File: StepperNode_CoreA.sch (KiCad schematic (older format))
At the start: 1 part

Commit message: Finished DAC interface sheets.
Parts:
- A?: symbol NODE_CORE_CONNECTOR -> NODE_CORE_CONNECTOR-RESCUE-rloopStepperNode
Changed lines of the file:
@@
 EESchema Schematic File Version 2
+LIBS:rloopStepperNode-rescue
 LIBS:power
 LIBS:device
@@
 Original Author: SafetyLok
 $Comp
-L NODE_CORE_CONNECTOR A?
+L NODE_CORE_CONNECTOR-RESCUE-rloopStepperNode A?
 U 1 1 57538837
 P 8150 4600

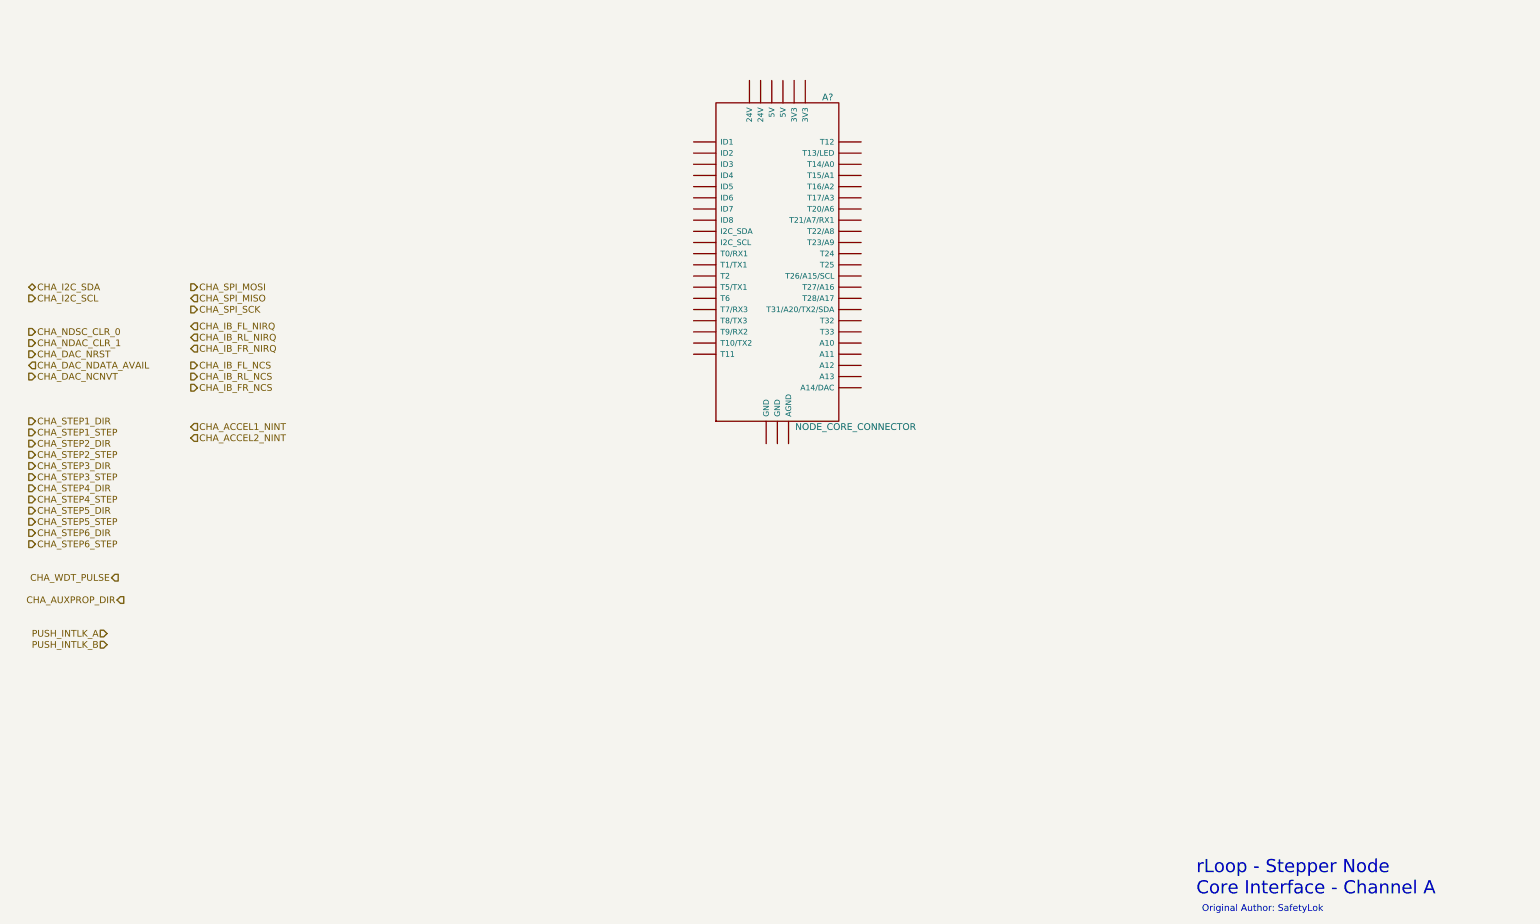
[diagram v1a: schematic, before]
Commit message: Updated node core connector pages and added interlocks.
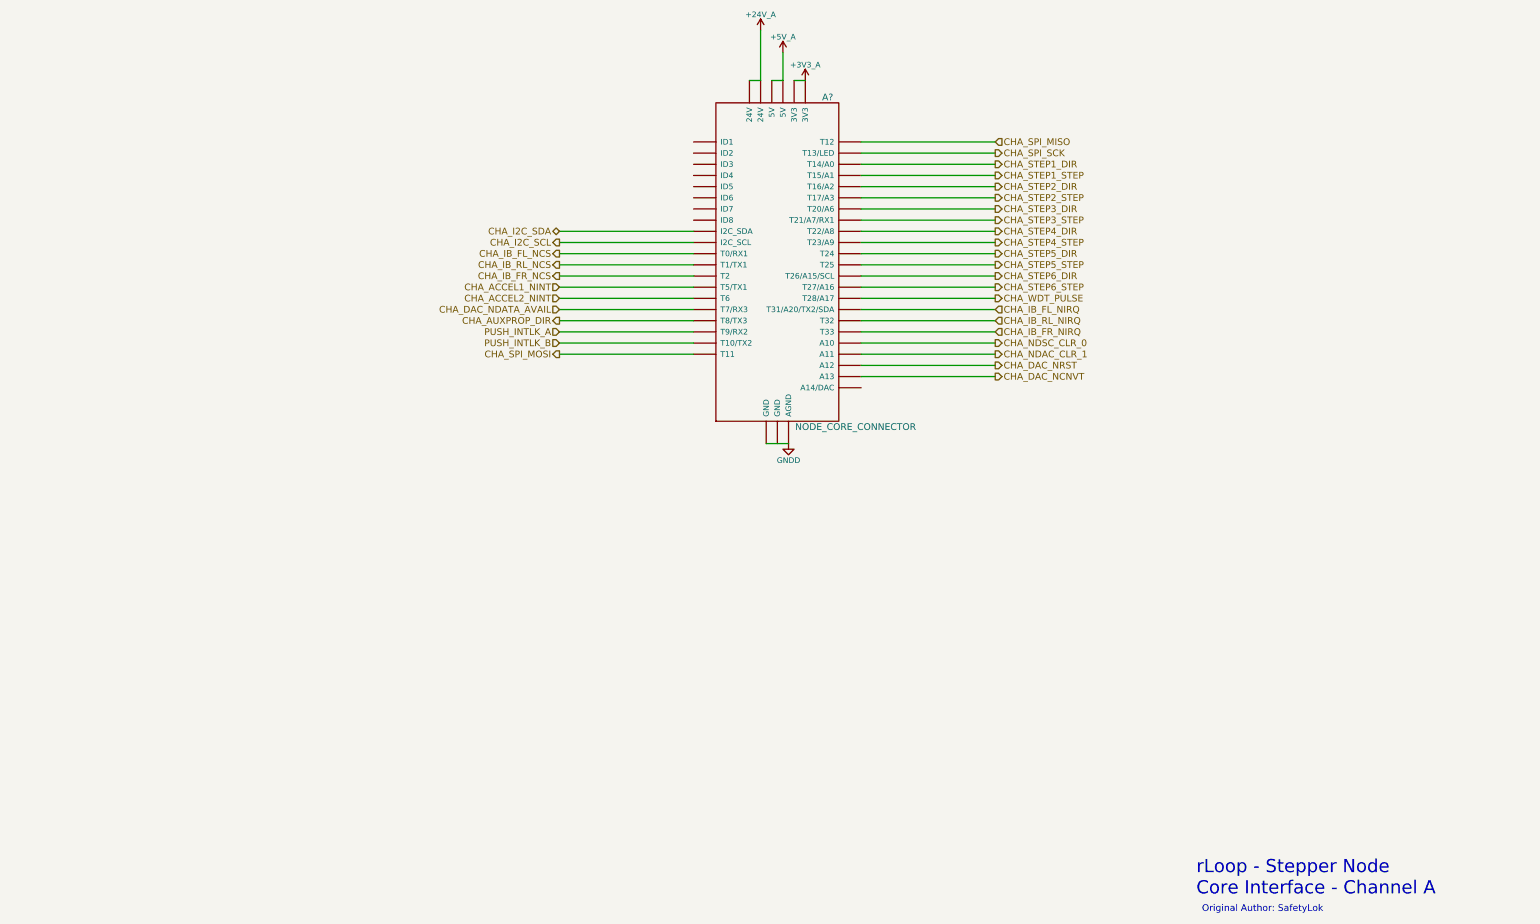
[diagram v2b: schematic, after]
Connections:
- net CHA_ACCEL1_NINT: now also A?.T5 (T5/TX1)
- net CHA_ACCEL2_NINT: now also A?.T6
- net CHA_AUXPROP_DIR: now also A?.T8 (T8/TX3)
- net CHA_DAC_NCNVT: now also A?.A13
- net CHA_DAC_NDATA_AVAIL: now also A?.T7 (T7/RX3)
- net CHA_DAC_NRST: now also A?.A12
- net CHA_I2C_SCL: now also A?.~ (ID8)
- net CHA_I2C_SDA: now also A?.~ (ID8)
- net CHA_IB_FL_NCS: now also A?.T0 (T0/RX1)
- net CHA_IB_FL_NIRQ: now also A?.T31 (T31/A20/TX2/SDA)
- net CHA_IB_FR_NCS: now also A?.T2
- net CHA_IB_FR_NIRQ: now also A?.T33
- net CHA_IB_RL_NCS: now also A?.T1 (T1/TX1)
- net CHA_IB_RL_NIRQ: now also A?.T32
- net CHA_NDAC_CLR_1: now also A?.A11
- net CHA_NDSC_CLR_0: now also A?.A10
- net CHA_SPI_MISO: now also A?.T12
- net CHA_SPI_MOSI: now also A?.T11
- net CHA_SPI_SCK: now also A?.T13 (T13/LED)
- net CHA_STEP1_DIR: now also A?.T14 (T14/A0)
- net CHA_STEP1_STEP: now also A?.T15 (T15/A1)
- net CHA_STEP2_DIR: now also A?.T16 (T16/A2)
- net CHA_STEP2_STEP: now also A?.T17 (T17/A3)
- net CHA_STEP3_DIR: now also A?.T20 (T20/A6)
- net CHA_STEP3_STEP: now also A?.T21 (T21/A7/RX1)
- net CHA_STEP4_DIR: now also A?.T22 (T22/A8)
- net CHA_STEP4_STEP: now also A?.T23 (T23/A9)
- net CHA_STEP5_DIR: now also A?.T24
- net CHA_STEP5_STEP: now also A?.T25
- net CHA_STEP6_DIR: now also A?.T26 (T26/A15/SCL)
- net CHA_STEP6_STEP: now also A?.T27 (T27/A16)
- net CHA_WDT_PULSE: now also A?.T28 (T28/A17)
- net PUSH_INTLK_A: now also A?.T9 (T9/RX2)
- net PUSH_INTLK_B: now also A?.T10 (T10/TX2)
- net +5V: now reaches A?.+24V (24V)
- net +5V: now also A?.+5V (5V)
- net +3V3: now reaches A?.+3V3 (3V3)
- net GNDD: now reaches A?.AGND
- net GNDD: now also A?.GND
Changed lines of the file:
@@
 	1    0    0    -1
 $EndComp
-Text HLabel 1450 4900 2    60   BiDi ~ 0
+Text HLabel 10100 5400 2    60   Output ~ 0
+CHA_NDSC_CLR_0
+Text HLabel 10100 5500 2    60   Output ~ 0
+CHA_NDAC_CLR_1
+Text HLabel 10100 5600 2    60   Output ~ 0
+CHA_DAC_NRST
+Text HLabel 6200 5100 0    60   Input ~ 0
+CHA_DAC_NDATA_AVAIL
+Text HLabel 10100 5700 2    60   Output ~ 0
+CHA_DAC_NCNVT
+Text HLabel 10100 3800 2    60   Output ~ 0
+CHA_STEP1_DIR
+Text HLabel 10100 3900 2    60   Output ~ 0
+CHA_STEP1_STEP
+Text HLabel 10100 4000 2    60   Output ~ 0
+CHA_STEP2_DIR
+Text HLabel 10100 4100 2    60   Output ~ 0
+CHA_STEP2_STEP
+Text HLabel 10100 4200 2    60   Output ~ 0
+CHA_STEP3_DIR
+Text HLabel 10100 4300 2    60   Output ~ 0
+CHA_STEP3_STEP
+Text HLabel 10100 4400 2    60   Output ~ 0
+CHA_STEP4_DIR
+Text HLabel 10100 4500 2    60   Output ~ 0
+CHA_STEP4_STEP
+Text HLabel 10100 4600 2    60   Output ~ 0
+CHA_STEP5_DIR
+Text HLabel 10100 4700 2    60   Output ~ 0
+CHA_STEP5_STEP
+Text HLabel 10100 4800 2    60   Output ~ 0
+CHA_STEP6_DIR
+Text HLabel 10100 4900 2    60   Output ~ 0
+CHA_STEP6_STEP
+Text HLabel 10100 5000 2    60   Output ~ 0
+CHA_WDT_PULSE
+Text HLabel 10100 5100 2    60   Input ~ 0
+CHA_IB_FL_NIRQ
+Text HLabel 10100 5200 2    60   Input ~ 0
+CHA_IB_RL_NIRQ
+Text HLabel 10100 5300 2    60   Input ~ 0
+CHA_IB_FR_NIRQ
+Text HLabel 6200 4700 0    60   Output ~ 0
+CHA_IB_RL_NCS
+Text HLabel 6200 4800 0    60   Output ~ 0
+CHA_IB_FR_NCS
+Text HLabel 6200 4600 0    60   Output ~ 0
+CHA_IB_FL_NCS
+Text HLabel 6200 5500 0    60   Output ~ 0
+CHA_SPI_MOSI
+Text HLabel 6200 5200 0    60   Output ~ 0
+CHA_AUXPROP_DIR
+Text HLabel 6200 5300 0    60   Input ~ 0
+PUSH_INTLK_A
+Text HLabel 6200 5400 0    60   Input ~ 0
+PUSH_INTLK_B
+Text HLabel 6200 4900 0    60   Input ~ 0
+CHA_ACCEL1_NINT
+Text HLabel 6200 5000 0    60   Input ~ 0
+CHA_ACCEL2_NINT
+$Comp
+L +3V3_A #PWR?
+U 1 1 575DF18E
+P 8400 3050
+F 0 "#PWR?" H 8400 2900 50  0001 C CNN
+F 1 "+3V3_A" H 8400 3190 50  0000 C CNN
+F 2 "" H 8400 3050 60  0000 C CNN
+F 3 "" H 8400 3050 60  0000 C CNN
+	1    8400 3050
+	1    0    0    -1
+$EndComp
+$Comp
+L +5V_A #PWR?
+U 1 1 575DF1A4
+P 8200 2800
+F 0 "#PWR?" H 8200 2650 50  0001 C CNN
+F 1 "+5V_A" H 8200 2940 50  0000 C CNN
+F 2 "" H 8200 2800 60  0000 C CNN
+F 3 "" H 8200 2800 60  0000 C CNN
+	1    8200 2800
+	1    0    0    -1
+$EndComp
+$Comp
+L +24V_A #PWR?
+U 1 1 575DF1BA
+P 8000 2600
+F 0 "#PWR?" H 8000 2450 50  0001 C CNN
+F 1 "+24V_A" H 8000 2740 50  0000 C CNN
+F 2 "" H 8000 2600 60  0000 C CNN
+F 3 "" H 8000 2600 60  0000 C CNN
+	1    8000 2600
+	1    0    0    -1
+$EndComp
+Wire Wire Line
+	8000 2600 8000 3050
+Wire Wire Line
+	8000 3050 7900 3050
+Wire Wire Line
+	8200 2800 8200 3050
+Wire Wire Line
+	8200 3050 8100 3050
+Wire Wire Line
+	8300 3050 8400 3050
+$Comp
+L GNDD #PWR?
+U 1 1 575DF220
+P 8250 6300
+F 0 "#PWR?" H 8250 6050 50  0001 C CNN
+F 1 "GNDD" H 8250 6150 50  0000 C CNN
+F 2 "" H 8250 6300 50  0000 C CNN
+F 3 "" H 8250 6300 50  0000 C CNN
+	1    8250 6300
+	1    0    0    -1
+$EndComp
+Wire Wire Line
+	8050 6300 8250 6300
+Wire Wire Line
+	7400 4400 6200 4400
+Wire Wire Line
+	7400 4500 6200 4500
+Text HLabel 6200 4400 0    60   BiDi ~ 0
 CHA_I2C_SDA
-Text HLabel 1450 5000 2    60   Output ~ 0
+Text HLabel 6200 4500 0    60   Output ~ 0
 CHA_I2C_SCL
-Text HLabel 1450 5300 2    60   Output ~ 0
-CHA_NDSC_CLR_0
-Text HLabel 1450 5400 2    60   Output ~ 0
-CHA_NDAC_CLR_1
-Text HLabel 1450 5500 2    60   Output ~ 0
-CHA_DAC_NRST
-Text HLabel 1450 5600 2    60   Input ~ 0
-CHA_DAC_NDATA_AVAIL
-Text HLabel 1450 5700 2    60   Output ~ 0
-CHA_DAC_NCNVT
-Text HLabel 1450 6100 2    60   Output ~ 0
-CHA_STEP1_DIR
-Text HLabel 1450 6200 2    60   Output ~ 0
-CHA_STEP1_STEP
-Text HLabel 1450 6300 2    60   Output ~ 0
-CHA_STEP2_DIR
-Text HLabel 1450 6400 2    60   Output ~ 0
-CHA_STEP2_STEP
-Text HLabel 1450 6500 2    60   Output ~ 0
-CHA_STEP3_DIR
-Text HLabel 1450 6600 2    60   Output ~ 0
-CHA_STEP3_STEP
-Text HLabel 1450 6700 2    60   Output ~ 0
-CHA_STEP4_DIR
-Text HLabel 1450 6800 2    60   Output ~ 0
-CHA_STEP4_STEP
-Text HLabel 1450 6900 2    60   Output ~ 0
-CHA_STEP5_DIR
-Text HLabel 1450 7000 2    60   Output ~ 0
-CHA_STEP5_STEP
-Text HLabel 1450 7100 2    60   Output ~ 0
-CHA_STEP6_DIR
-Text HLabel 1450 7200 2    60   Output ~ 0
-CHA_STEP6_STEP
-Text HLabel 2250 7500 0    60   Output ~ 0
-CHA_WDT_PULSE
-Text HLabel 2900 5250 2    60   Input ~ 0
-CHA_IB_FL_NIRQ
-Text HLabel 2900 5350 2    60   Input ~ 0
-CHA_IB_RL_NIRQ
-Text HLabel 2900 5450 2    60   Input ~ 0
-CHA_IB_FR_NIRQ
-Text HLabel 2900 5700 2    60   Output ~ 0
-CHA_IB_RL_NCS
-Text HLabel 2900 5800 2    60   Output ~ 0
-CHA_IB_FR_NCS
-Text HLabel 2900 5600 2    60   Output ~ 0
-CHA_IB_FL_NCS
-Text HLabel 2900 4900 2    60   Output ~ 0
-CHA_SPI_MOSI
-Text HLabel 2900 5000 2    60   Input ~ 0
+Wire Wire Line
+	7400 4600 6200 4600
+Wire Wire Line
+	7400 4700 6200 4700
+Wire Wire Line
+	7400 4800 6200 4800
+Wire Wire Line
+	7400 5500 6200 5500
+Wire Wire Line
+	10100 3600 8900 3600
+Wire Wire Line
+	10100 3700 8900 3700
+Text HLabel 10100 3600 2    60   Input ~ 0
 CHA_SPI_MISO
-Text HLabel 2900 5100 2    60   Output ~ 0
+Text HLabel 10100 3700 2    60   Output ~ 0
 CHA_SPI_SCK
-Text HLabel 2300 7700 0    60   Output ~ 0
-CHA_AUXPROP_DIR
-Text HLabel 2150 8000 0    60   Input ~ 0
-PUSH_INTLK_A
-Text HLabel 2150 8100 0    60   Input ~ 0
-PUSH_INTLK_B
-Text HLabel 2900 6150 2    60   Input ~ 0
-CHA_ACCEL1_NINT
-Text HLabel 2900 6250 2    60   Input ~ 0
-CHA_ACCEL2_NINT
+Wire Wire Line
+	10100 3800 8900 3800
+Wire Wire Line
+	10100 3900 8900 3900
+Wire Wire Line
+	10100 4000 8900 4000
+Wire Wire Line
+	10100 4100 8900 4100
+Wire Wire Line
+	10100 4200 8900 4200
+Wire Wire Line
+	10100 4300 8900 4300
+Wire Wire Line
+	10100 4400 8900 4400
+Wire Wire Line
+	10100 4500 8900 4500
+Wire Wire Line
+	10100 4600 8900 4600
+Wire Wire Line
+	10100 5100 8900 5100
+Wire Wire Line
+	10100 5200 8900 5200
+Wire Wire Line
+	10100 5300 8900 5300
+Wire Wire Line
+	10100 4700 8900 4700
+Wire Wire Line
+	10100 4800 8900 4800
+Wire Wire Line
+	10100 4900 8900 4900
+Wire Wire Line
+	10100 5000 8900 5000
+Wire Wire Line
+	10100 5500 8900 5500
+Wire Wire Line
+	10100 5600 8900 5600
+Wire Wire Line
+	10100 5700 8900 5700
+Wire Wire Line
+	10100 5400 8900 5400
+Wire Wire Line
+	7400 4900 6200 4900
+Wire Wire Line
+	7400 5000 6200 5000
+Wire Wire Line
+	7400 5100 6200 5100
+Wire Wire Line
+	7400 5200 6200 5200
+Wire Wire Line
+	7400 5300 6200 5300
+Wire Wire Line
+	7400 5400 6200 5400
 $EndSCHEMATC

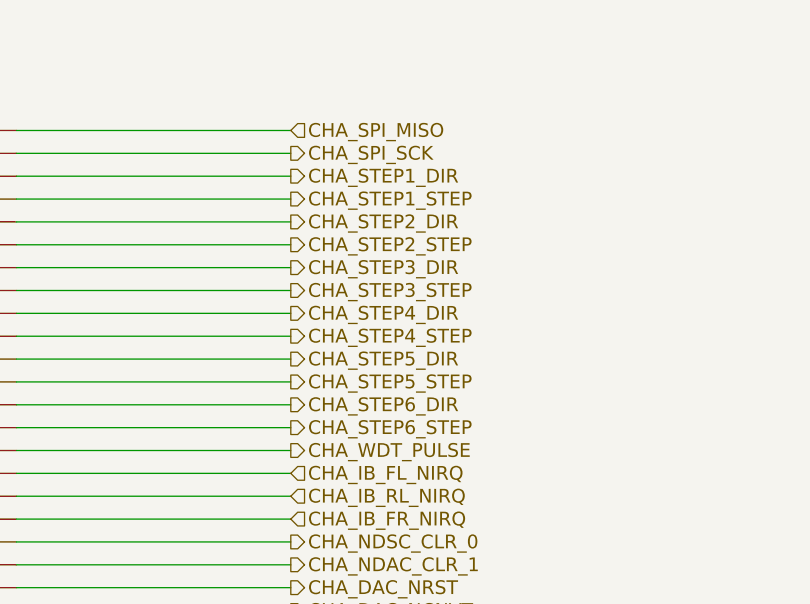
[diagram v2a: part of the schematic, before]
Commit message: Remove Gimbal Functions
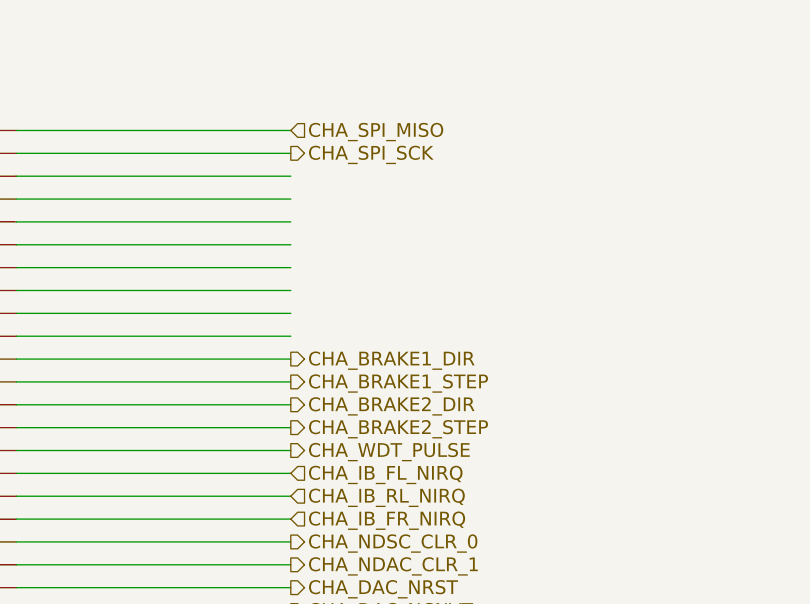
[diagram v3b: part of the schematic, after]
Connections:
- net labels added: CHA_BRAKE1_DIR, CHA_BRAKE1_STEP, CHA_BRAKE2_DIR, CHA_BRAKE2_STEP
- net labels removed: CHA_STEP1_DIR, CHA_STEP1_STEP, CHA_STEP2_DIR, CHA_STEP2_STEP, CHA_STEP3_DIR, CHA_STEP3_STEP, CHA_STEP4_DIR, CHA_STEP4_STEP, CHA_STEP5_DIR, CHA_STEP5_STEP, CHA_STEP6_DIR, CHA_STEP6_STEP
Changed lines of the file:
@@
 $Descr A3 16535 11693
 encoding utf-8
-Sheet 8 17
+Sheet 4 15
 Title "Stepper Node - Core A"
 Date ""
@@
 Text HLabel 10100 5700 2    60   Output ~ 0
 CHA_DAC_NCNVT
-Text HLabel 10100 3800 2    60   Output ~ 0
-CHA_STEP1_DIR
-Text HLabel 10100 3900 2    60   Output ~ 0
-CHA_STEP1_STEP
-Text HLabel 10100 4000 2    60   Output ~ 0
-CHA_STEP2_DIR
-Text HLabel 10100 4100 2    60   Output ~ 0
-CHA_STEP2_STEP
-Text HLabel 10100 4200 2    60   Output ~ 0
-CHA_STEP3_DIR
-Text HLabel 10100 4300 2    60   Output ~ 0
-CHA_STEP3_STEP
-Text HLabel 10100 4400 2    60   Output ~ 0
-CHA_STEP4_DIR
-Text HLabel 10100 4500 2    60   Output ~ 0
-CHA_STEP4_STEP
 Text HLabel 10100 4600 2    60   Output ~ 0
-CHA_STEP5_DIR
+CHA_BRAKE1_DIR
 Text HLabel 10100 4700 2    60   Output ~ 0
-CHA_STEP5_STEP
+CHA_BRAKE1_STEP
 Text HLabel 10100 4800 2    60   Output ~ 0
-CHA_STEP6_DIR
+CHA_BRAKE2_DIR
 Text HLabel 10100 4900 2    60   Output ~ 0
-CHA_STEP6_STEP
+CHA_BRAKE2_STEP
 Text HLabel 10100 5000 2    60   Output ~ 0
 CHA_WDT_PULSE

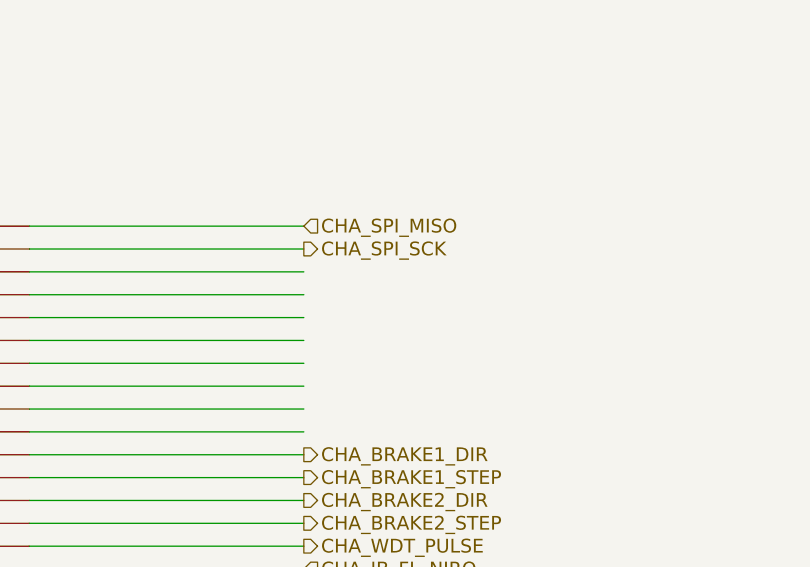
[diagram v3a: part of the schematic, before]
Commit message: Update DAC's and routed gimbal position to MCU direct.
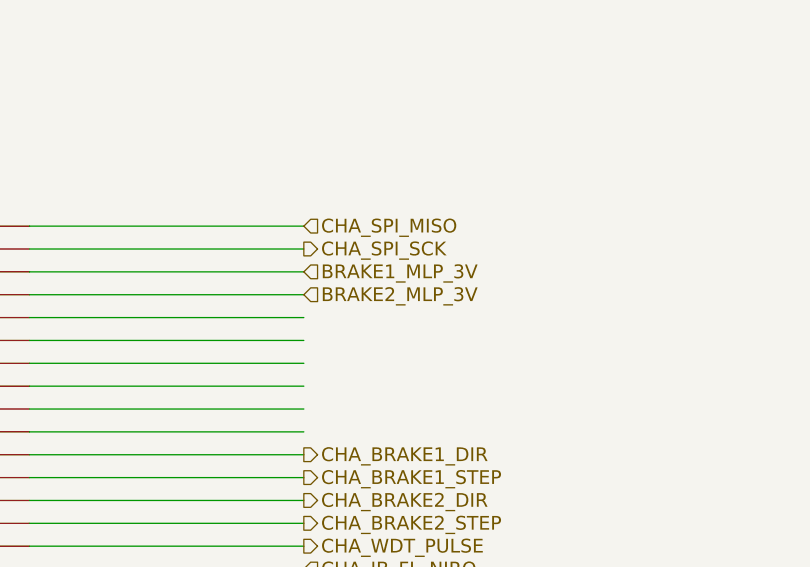
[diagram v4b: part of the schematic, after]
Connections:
- net labels added: BRAKE1_MLP_3V, BRAKE2_MLP_3V
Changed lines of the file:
@@
 Wire Wire Line
 	7400 5400 6200 5400
+Text HLabel 10100 3800 2    60   Input ~ 0
+BRAKE1_MLP_3V
+Text HLabel 10100 3900 2    60   Input ~ 0
+BRAKE2_MLP_3V
 $EndSCHEMATC
